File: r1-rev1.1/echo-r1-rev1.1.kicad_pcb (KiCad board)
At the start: 6 copper layers, 55 x 95 mm, 148 parts, among them J1 GT-BTP30003-xxxA-16A, J2 TYPE-C-31-M-12, J3 TF-115, J4 HP_3.5mm, J5 LO_3.5mm, J6 AFD01-S35FCC-00, J7 PM254-1-06-W-8.5, Q2 AO3401A, Q5 AO3401A, Q6 AO3401A, Q7 AO3401A, SW1 DPAD↑, SW10 X, SW11 Y, SW12 START, SW13 SELECT, SW14 HOLD, SW2 DPAD↓, SW3 DPAD←, SW4 DPAD→, SW5 A, SW6 B, SW7 VOL+, SW8 VOL-, SW9 POWER, U1 LM66100DCK, U10 AP2502, U2 TPS62A01DRLR, U3 TPS62A01DRLR, U4 XC6206P33xMR, U5 TP4057, U6 STM32H743IGTx, U7 W9825G6KH-x, U8 USB3320C-EZK, U9 TLV320AIC3104, Y1 SC-32S32.768kHz20PPM12.5pF, Y2 XTM32024000JT00351001

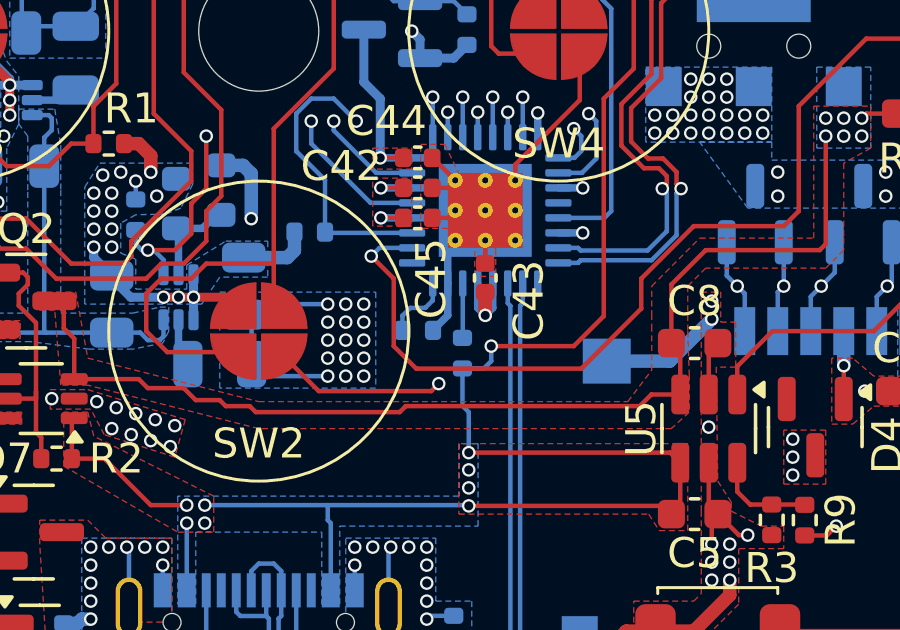
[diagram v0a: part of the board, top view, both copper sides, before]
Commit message: Fix USB3320C ID pin
The ID pin should be tied to VDD33 or left floating for
device mode. Tying to ground puts the PHY into host mode,
which requires a software workaround to get USB working.

See Github issue: #9
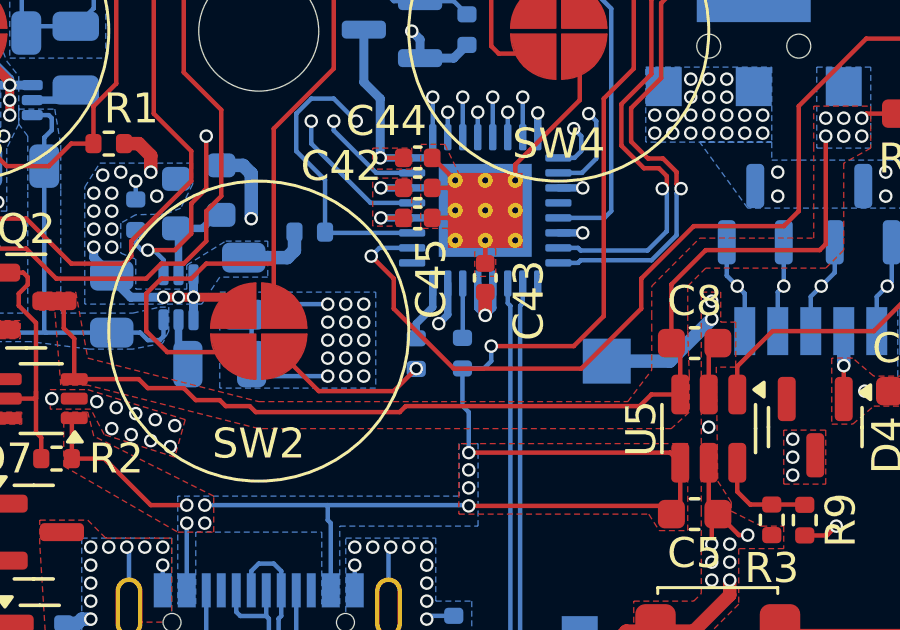
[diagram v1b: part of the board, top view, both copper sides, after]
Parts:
- moved R17 0.78 mm to (153.8, 137.8), turned to 90 degrees
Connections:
- U8 pad 23: GND -> 3V3
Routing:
- net GND: track 201.4 -> 197.6 mm
- net 3V3: track 86.7 -> 88.2 mm, vias 54 -> 55
- net /cpu/mcoclk_24m: track 55.4 -> 54.6 mm

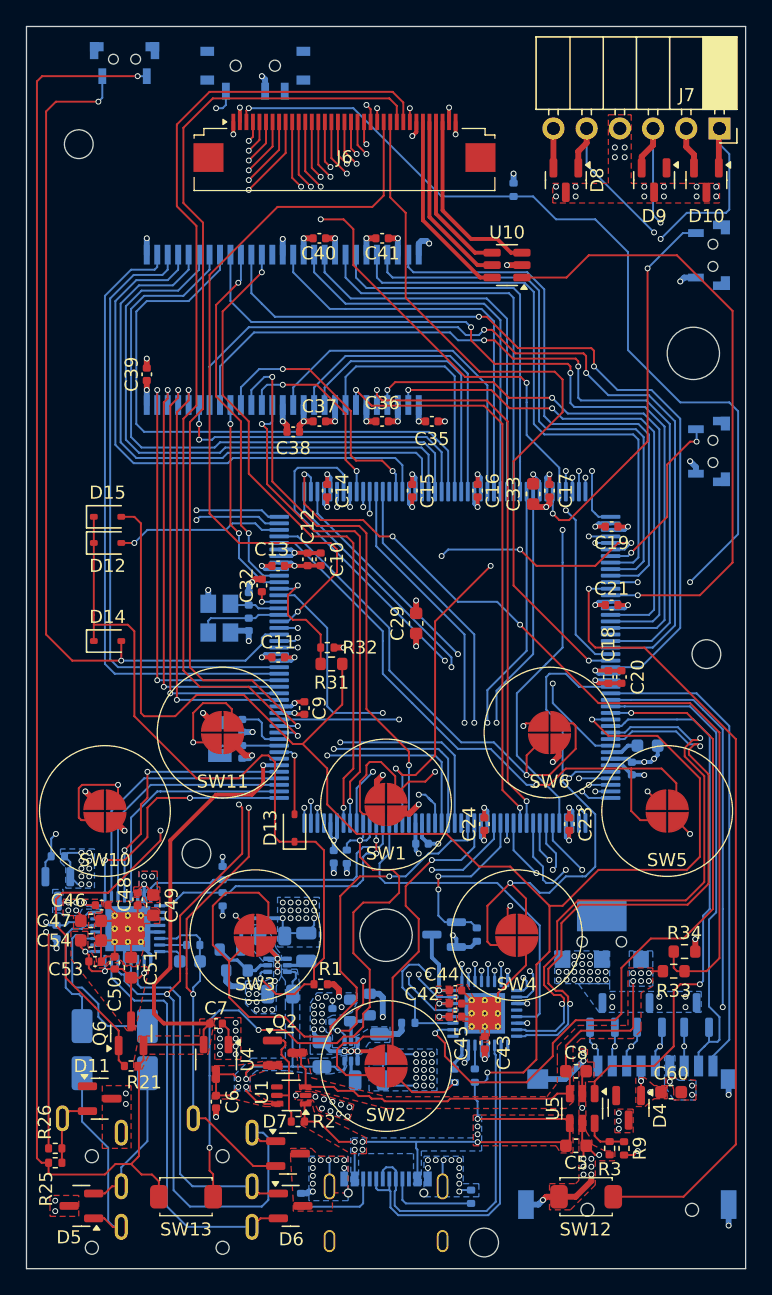
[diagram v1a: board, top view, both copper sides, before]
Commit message: Fix symbol library links & resync footprints from KiCAD libraries
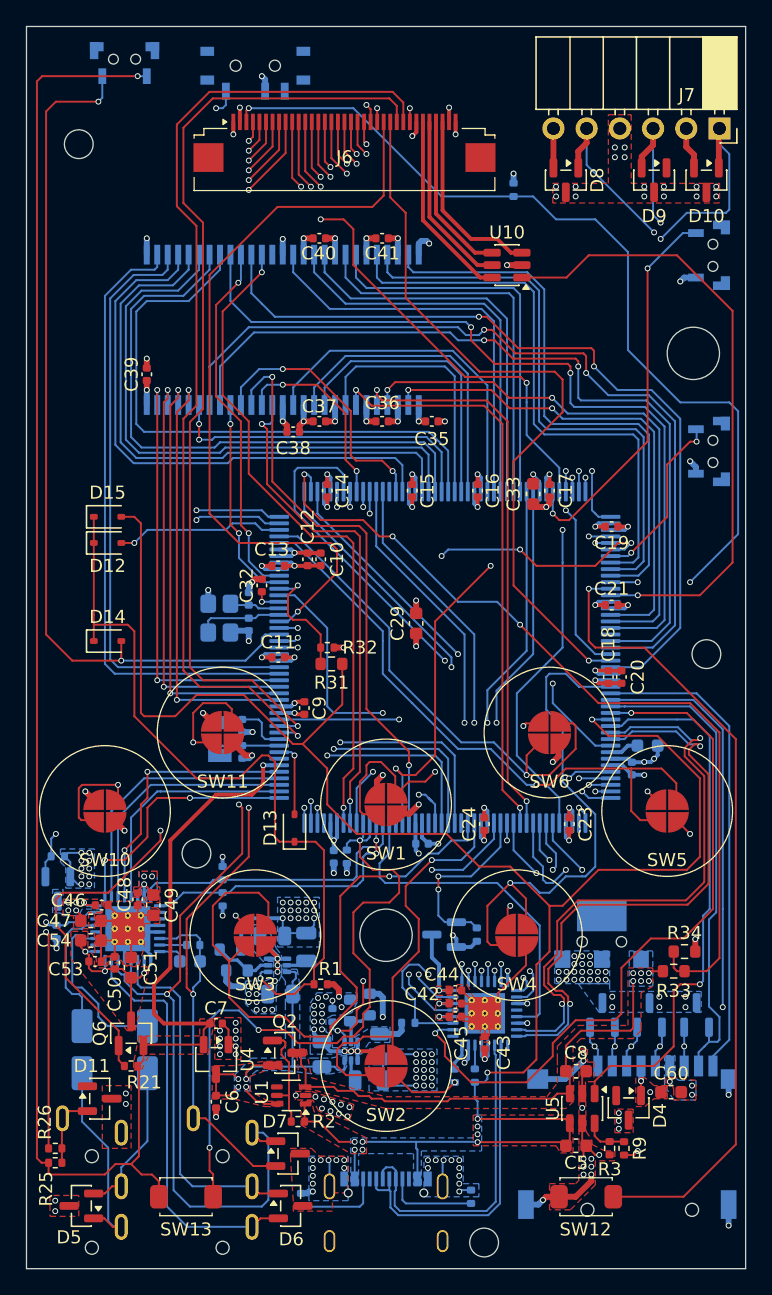
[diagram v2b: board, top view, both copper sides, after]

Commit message: Fix incorrect 3.5mm jack pinout
Document the R1-Rev1's wrong pinout properly and fix the pinout
in later revs so that jacks will work properly without needing
a custom adapter.

See Github issue: #12
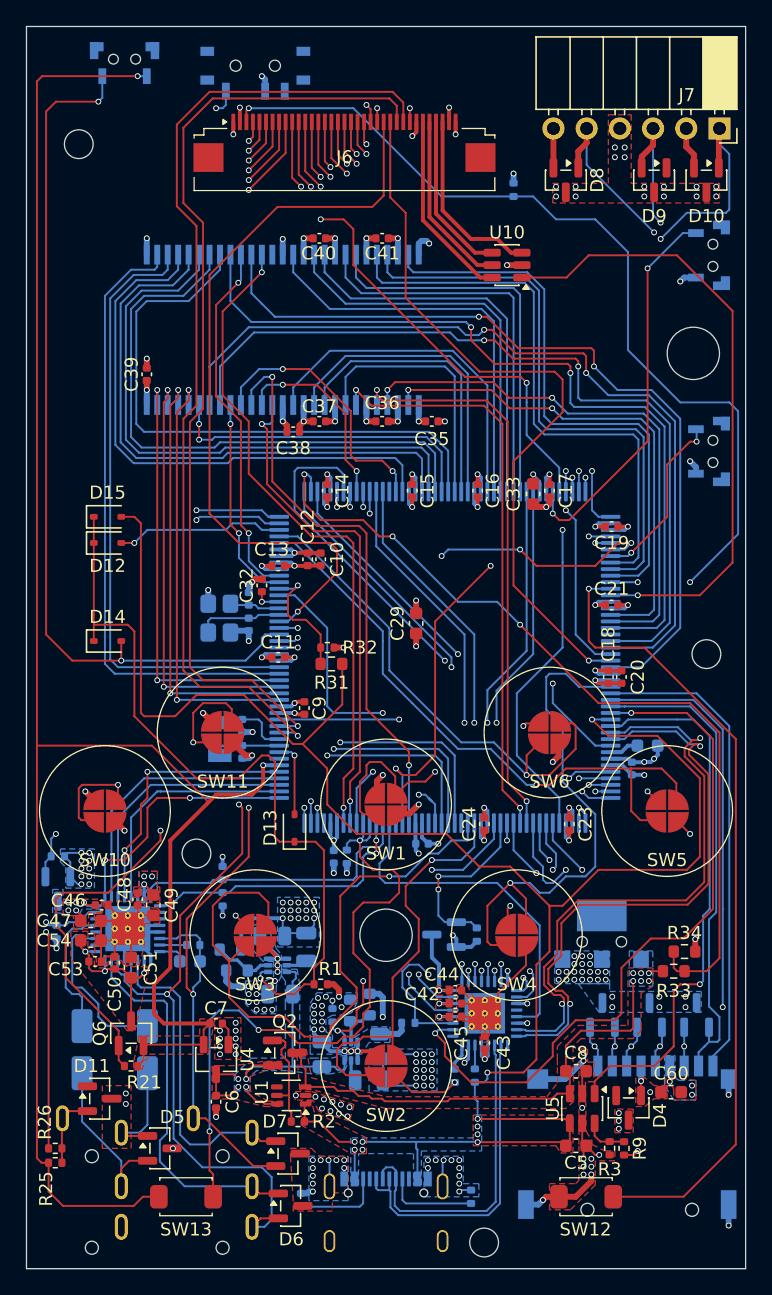
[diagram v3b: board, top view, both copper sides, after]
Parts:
- moved D5 7.44 mm to (131.2, 143.3), turned to 0 degrees
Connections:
- C55 pad 2: Net-(D5-IO2) -> Net-(D5-IO1)
- C56 pad 2: Net-(D5-IO1) -> Net-(D5-IO2)
- D6 pad 1: /audio/hp_left -> /audio/hp_right
- D6 pad 2: /audio/hp_right -> /audio/hp_com
- D7 pad 1: /audio/hp_com -> /audio/hp_left
- J5 pad R1: Net-(D5-IO1) -> Net-(D5-IO2)
- J5 pad T: Net-(D5-IO2) -> Net-(D5-IO1)
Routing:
- net Net-(D5-IO1): track 15.7 -> 8.31 mm
- net 3V3_LDO: track 149.1 -> 156.3 mm
- net /audio/hp_com: track 40.4 -> 36.2 mm
- net /audio/hp_left: track 27.1 -> 24.2 mm
- net /audio/hp_right: track 31.3 -> 28.7 mm
- net Net-(D5-IO2): track 11.8 -> 13.5 mm
- net GND: vias 188 -> 187

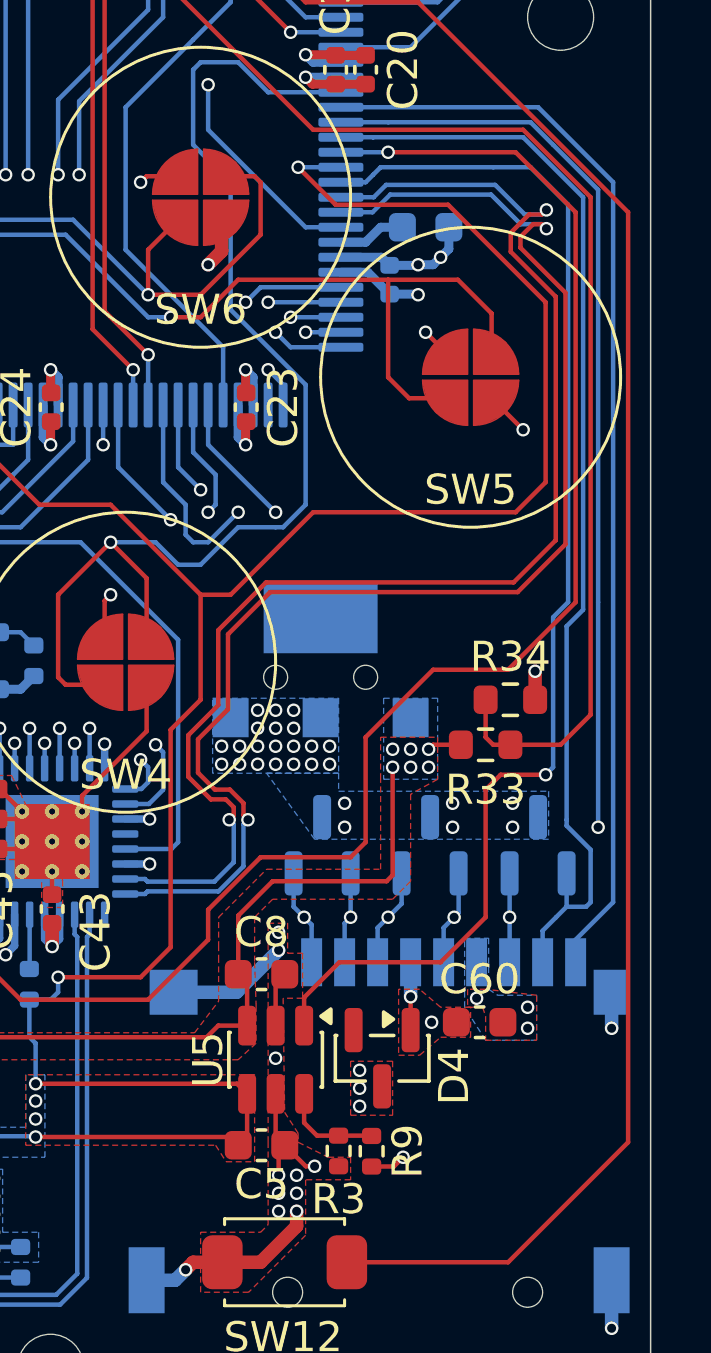
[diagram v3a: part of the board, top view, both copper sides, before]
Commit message: R1-Rev1.1: remove SDMMC ESD diodes and adjust routing
Remove the CESD3V3-AP ESD diodes and put a TODO to select
new diodes later. While here, reroute the SDMMC bus a bit
so it's not so messy.

See Github issue: #27
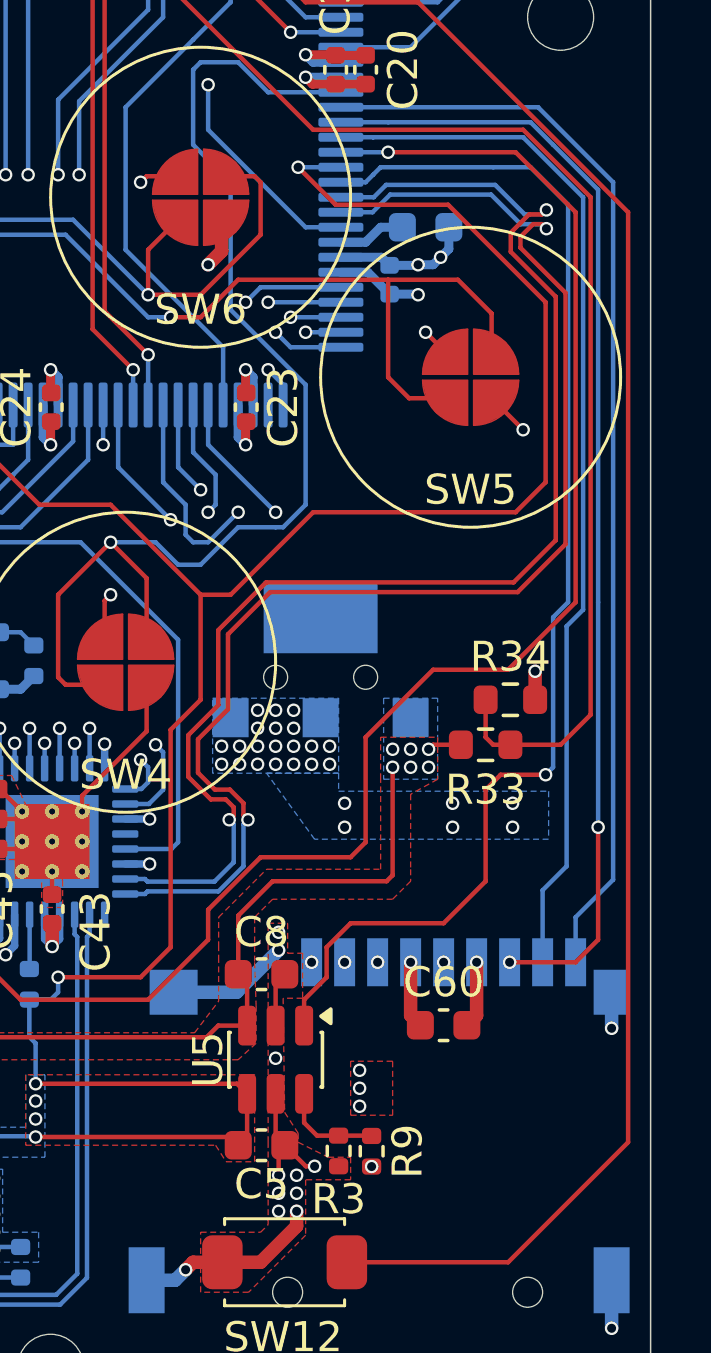
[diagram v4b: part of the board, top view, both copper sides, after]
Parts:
- removed D1, D2, D3, D4: CESD3V3AP-ES, Package_TO_SOT_SMD:SOT-23
- moved C60 1.20 mm to (169.1, 139.1)
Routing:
- net /cpu/sdmmc.cmd: track 32.3 -> 26.8 mm
- net GND: track 197.6 -> 199.9 mm, vias 187 -> 185
- net /cpu/sdmmc.d1: track 37.1 -> 35.0 mm
- net /cpu/sdmmc.d3: track 25.8 -> 23.6 mm
- net /cpu/sdmmc.d2: track 24.8 -> 22.9 mm
- net /cpu/sdmmc.clk: track 26.6 -> 24.7 mm
- net /cpu/~{charger_enable}: track 31.2 -> 32.7 mm
- net 3V3: track 88.2 -> 88.1 mm, vias 55 -> 54
